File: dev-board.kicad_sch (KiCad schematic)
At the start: 21 parts, among them J1 TYPE-C-31-M-12, J2 Conn_01x20_Pin, J3 Conn_01x20_Pin, SW1 TS-1088-AR02016, SW2 TS-1088-AR02016, U2 ESP32-S3-WROOM-1, U3 LD1117S33TR_SOT223

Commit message: Delete all crap
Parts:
- removed C1: 10u, Capacitor_SMD:C_0603_1608Metric, symbol Device:C
- removed C2: 22u, Capacitor_SMD:C_0603_1608Metric, symbol Device:C
- removed C3, C4: 100n, Capacitor_SMD:C_0603_1608Metric, symbol Device:C
- removed D1: RED, LED_SMD:LED_0603_1608Metric, symbol Device:LED
- removed D2: GREEN, LED_SMD:LED_0603_1608Metric, symbol Device:LED
- removed D3: BLUE, LED_SMD:LED_0603_1608Metric, symbol Device:LED
- removed J1: TYPE-C-31-M-12, TYPE-C-31-M-12:HRO_TYPE-C-31-M-12, symbol TYPE-C-31-M-12:TYPE-C-31-M-12
- removed J2, J3: Conn_01x20_Pin, Connector_PinHeader_2.54mm:PinHeader_1x20_P2.54mm_Vertical, symbol Connector:Conn_01x20_Pin
- removed R1, R2, R4, R5, R6: 5.1K, Resistor_SMD:R_0603_1608Metric, symbol Device:R
- removed U3: LD1117S33TR_SOT223, Package_TO_SOT_SMD:SOT-223-3_TabPin2, symbol Regulator_Linear:LD1117S33TR_SOT223
- renumbered U2 to U1
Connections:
- net +3V3: no longer R3.1
- net EN: no longer C5.1
- net GND: no longer C5.2
- new net +3.3V: R3.1
- no-connect marks 2 -> 0
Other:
- added sheet Power Circuits (power_circuits.kicad_sch)
- company: (none) -> Helmut Rohde GmbH

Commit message: Minor Changes
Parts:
- removed C5: 1u, Capacitor_SMD:C_0603_1608Metric, symbol Device:C
- removed R3: 5.1K, Resistor_SMD:R_0603_1608Metric, symbol Device:R
- removed SW1, SW2: TS-1088-AR02016, easyeda2kicad:SW-SMD_L3.9-W3.0-P4.45, symbol easyeda2kicad:TS-1088-AR02016
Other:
- moved on the sheet: U1

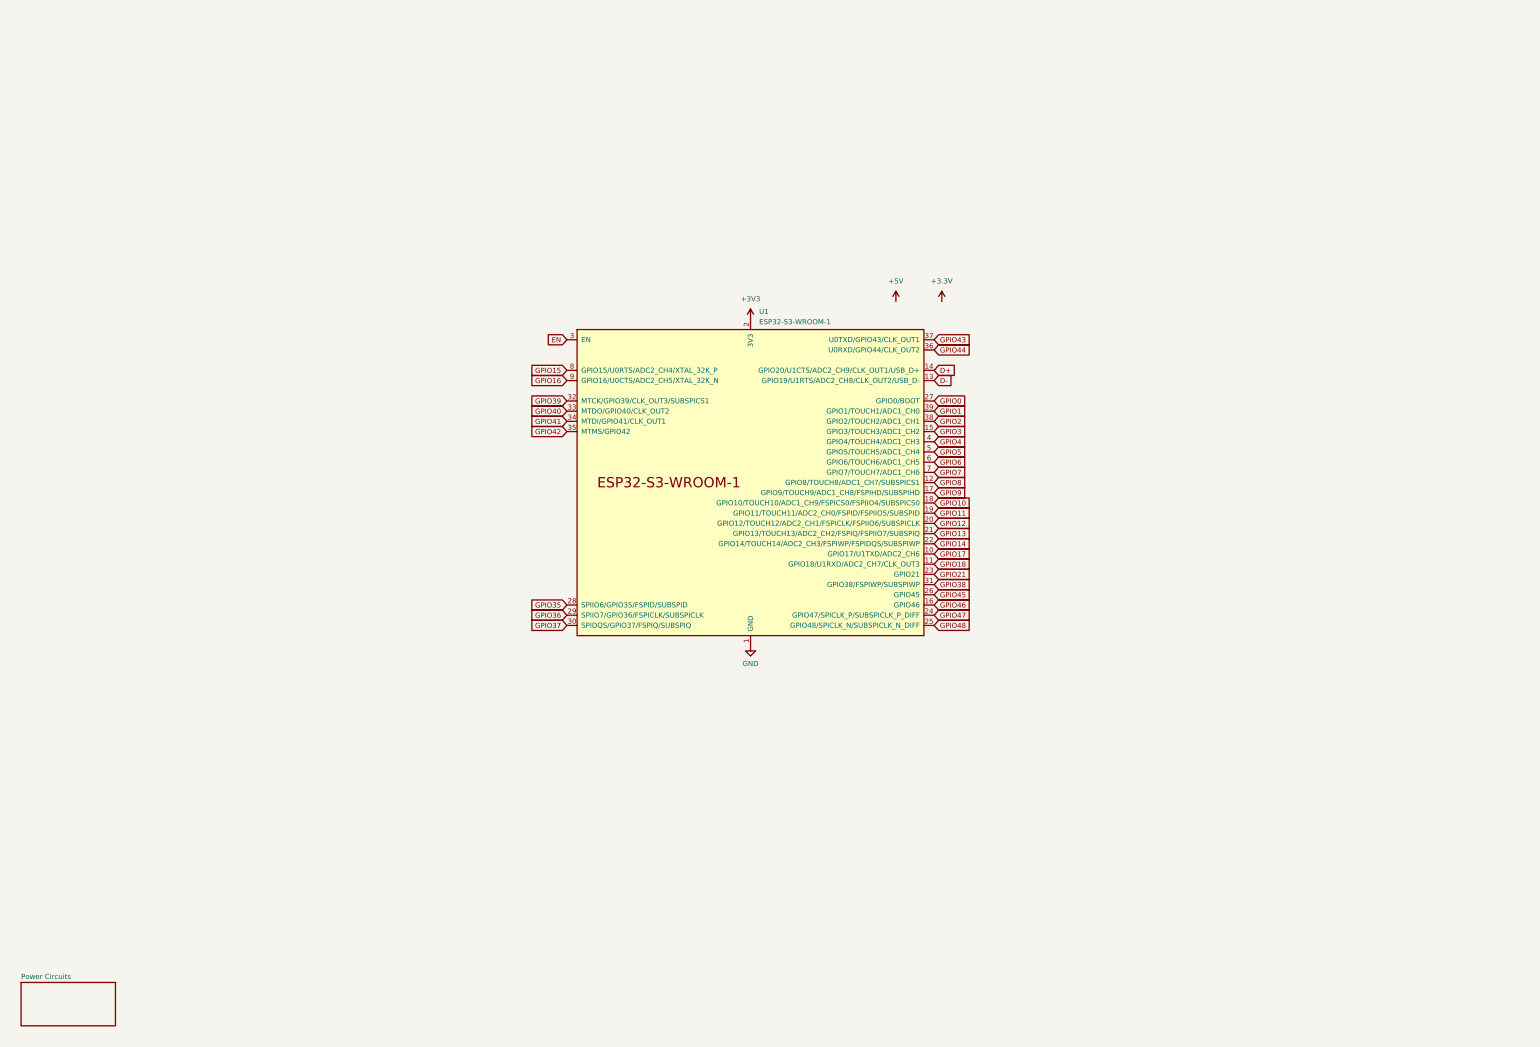
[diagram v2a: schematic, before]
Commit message: Copy and Adjust Parts from previous version
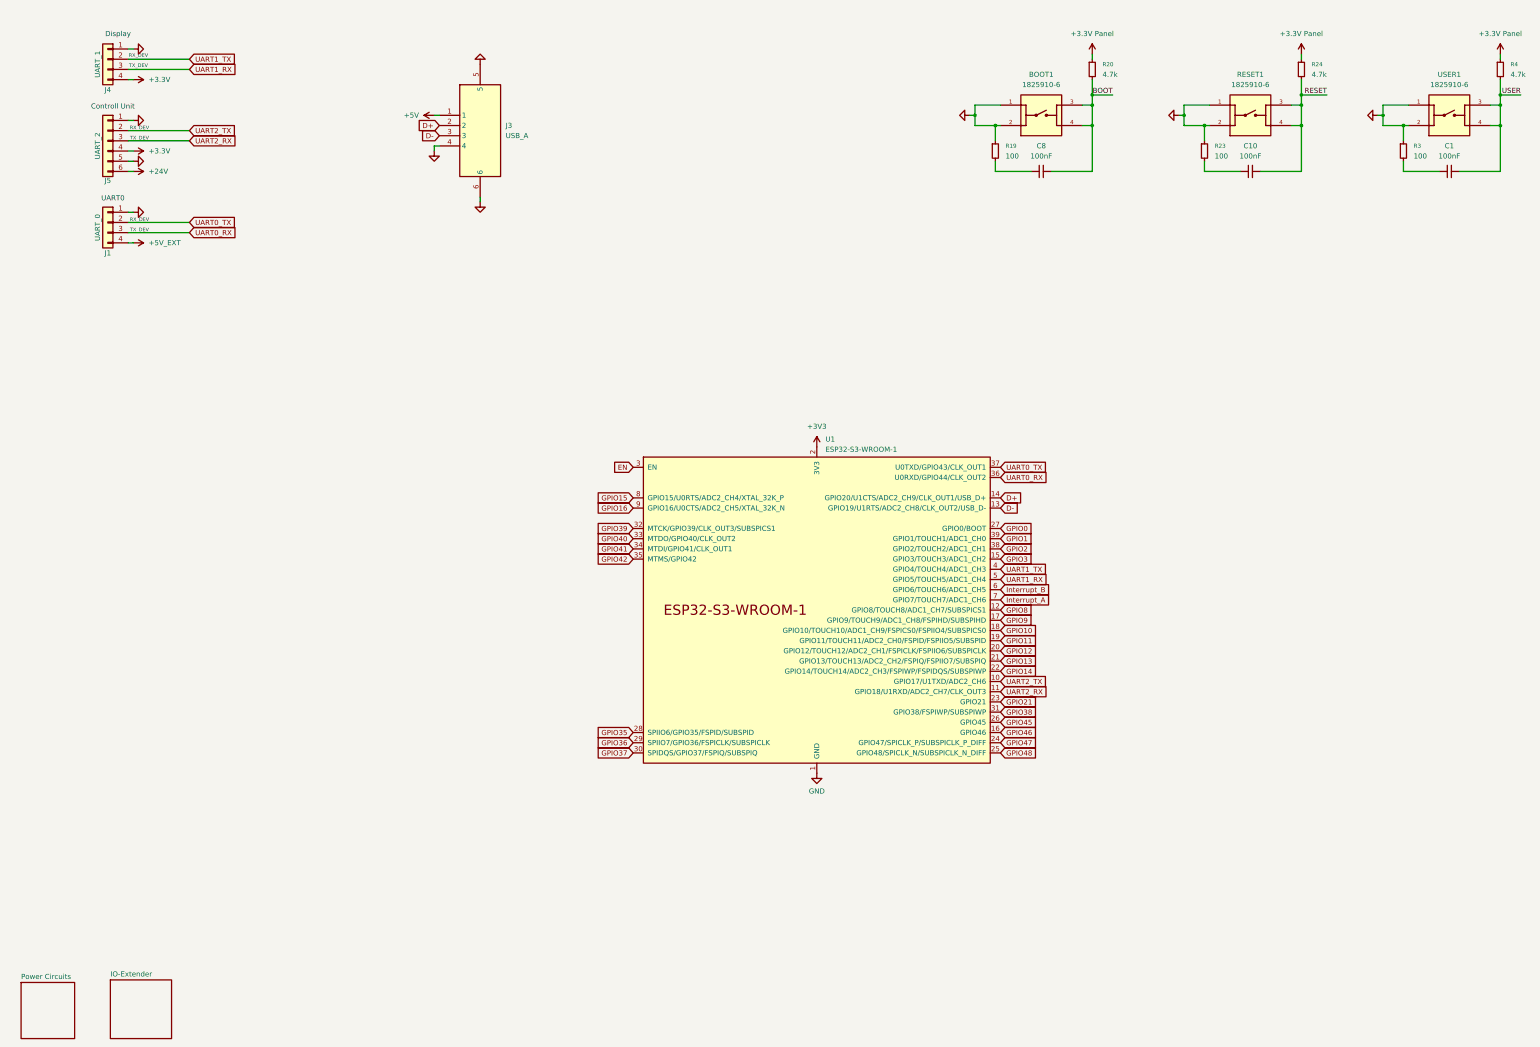
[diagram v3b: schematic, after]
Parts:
- added BOOT1, RESET1, USER1: 1825910-6, Switch 1825910_6:SW_1825910-6-4, symbol Switch 1825910-6:1825910-6
- added C1, C10, C8: 100nF, Capacitor_SMD:C_1206_3216Metric, symbol Device:C_Small
- added J1: UART_0, Connector_JST:JST_XH_B4B-XH-A_1x04_P2.50mm_Vertical, symbol Connector_Generic:Conn_01x04
- added J3: USB_A, SamacSys_Parts:USB-2.0-TYPE-A, symbol SamacSys_Parts:614004190021
- added J4: UART_1, Connector_JST:JST_XH_B4B-XH-A_1x04_P2.50mm_Vertical, symbol Connector_Generic:Conn_01x04
- added J5: UART_2, Connector_JST:JST_XH_S6B-XH-A-1_1x06_P2.50mm_Horizontal, symbol Connector_Generic:Conn_01x06
- added R19, R23, R3: 100, Resistor_SMD:R_1206_3216Metric, symbol Device:R_Small
- added R20, R24, R4: 4.7k, Resistor_SMD:R_1206_3216Metric, symbol Device:R_Small
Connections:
- net +3.3V: now also J4.4 (Pin_4), J5.4 (Pin_4)
- net +5V: now also J3.1
- net D+: now also J3.2
- net D-: now also J3.3
- net GND: now also J1.1 (Pin_1), J3.4, J3.5, J3.6, J4.1 (Pin_1), J5.1 (Pin_1), J5.5 (Pin_5)
- net GPIO17 renamed UART2_TX
- net UART2_TX: now also J5.2 (Pin_2)
- net GPIO18 renamed UART2_RX
- net UART2_RX: now also J5.3 (Pin_3)
- net GPIO4 renamed UART1_TX
- net UART1_TX: now also J4.2 (Pin_2)
- net GPIO43 renamed UART0_TX
- net UART0_TX: now also J1.2 (Pin_2)
- net GPIO44 renamed UART0_RX
- net UART0_RX: now also J1.3 (Pin_3)
- net GPIO5 renamed UART1_RX
- net UART1_RX: now also J4.3 (Pin_3)
- net GPIO6 renamed Interrupt_B
- net GPIO7 renamed Interrupt_A
- new net: C8.1, R19.2
- new net: C1.1, R3.2
- new net: C10.1, R23.2
- new net +24V: J5.6 (Pin_6)
- new net +3.3V Panel: R20.1, R24.1, R4.1
- new net +5V_EXT: J1.4 (Pin_4)
- new net BOOT: BOOT1.3, BOOT1.4, C8.2, R20.2
- new net GND Panel: BOOT1.1, BOOT1.2, R19.1, R23.1, R3.1, RESET1.1, RESET1.2, USER1.1, USER1.2
- new net RESET: C10.2, R24.2, RESET1.3, RESET1.4
- new net USER: C1.2, R4.2, USER1.3, USER1.4
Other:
- added sheet IO-Extender (io_extender.kicad_sch)
- note added: "Controll Unit"
- note added: "Display"
- note added: "RX_DEV"
- note added: "TX_DEV"
- note added: "UART0"
- moved on the sheet: U1
